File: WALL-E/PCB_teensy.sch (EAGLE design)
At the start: 44 parts

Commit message: added silkscreen to i2c headers
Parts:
- renumbered U$4 to U4
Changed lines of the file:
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@@
 <parts>
 <part name="U$2" library="WALL-E_Parts" deviceset="TACTILE-SWITCH-1825910-7" device=""/>
-<part name="U$4" library="WALL-E_Parts" deviceset="R-78E5.0-0.5" device=""/>
+<part name="U4" library="WALL-E_Parts" deviceset="R-78E5.0-0.5" device=""/>
 <part name="U$5" library="WALL-E_Parts" deviceset="LM3940" device=""/>
 <part name="U$6" library="adafruit" library_urn="urn:adsk.eagle:library:420" deviceset="2.1MMJACK" device="THM"/>
@@
 <instances>
 <instance part="U$2" gate="G$1" x="60.96" y="15.24"/>
-<instance part="U$4" gate="G$1" x="-93.98" y="48.26"/>
+<instance part="U4" gate="G$1" x="-93.98" y="48.26"/>
 <instance part="U$5" gate="G$1" x="-58.42" y="43.18"/>
 <instance part="U$6" gate="G$1" x="-124.46" y="71.12"/>
@@
 <pinref part="U$6" gate="G$1" pin="RING"/>
 <wire x1="-119.38" y1="63.5" x2="-119.38" y2="68.58" width="0.1524" layer="91"/>
-<pinref part="U$4" gate="G$1" pin="VIN"/>
+<pinref part="U4" gate="G$1" pin="VIN"/>
 <wire x1="-119.38" y1="68.58" x2="-109.22" y2="68.58" width="0.1524" layer="91"/>
 <wire x1="-109.22" y1="68.58" x2="-106.68" y2="68.58" width="0.1524" layer="91"/>
@@
 <net name="5V" class="0">
 <segment>
-<pinref part="U$4" gate="G$1" pin="VOUT"/>
+<pinref part="U4" gate="G$1" pin="VOUT"/>
 <wire x1="-81.28" y1="48.26" x2="-76.2" y2="48.26" width="0.1524" layer="91"/>
 <wire x1="-76.2" y1="48.26" x2="-76.2" y2="83.82" width="0.1524" layer="91"/>
@@
 <net name="N$1" class="0">
 <segment>
-<pinref part="U$4" gate="G$1" pin="GND"/>
+<pinref part="U4" gate="G$1" pin="GND"/>
 <pinref part="C4" gate="G$1" pin="1"/>
 <pinref part="TP13" gate="G$1" pin="TP"/>

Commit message: Finished labeling the silkscreen for everything.
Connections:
- removed net N$8: J2.2
- net GND: now also J2.2
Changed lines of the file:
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@@
 <label x="35.56" y="27.94" size="1.778" layer="95"/>
+</segment>
+<segment>
+<pinref part="J2" gate="G$1" pin="2"/>
+<wire x1="-48.26" y1="104.14" x2="-48.26" y2="99.06" width="0.1524" layer="91"/>
 </segment>
 </net>
@@
 </segment>
 </net>
-<net name="N$8" class="0">
-<segment>
-<pinref part="J2" gate="G$1" pin="2"/>
-<wire x1="-48.26" y1="104.14" x2="-48.26" y2="99.06" width="0.1524" layer="91"/>
-</segment>
-</net>

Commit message: removed some test pins
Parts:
- removed TP1, TP3: PTR1B2,54, testpad:PTR1B2,54
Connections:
- net +12V: no longer TP1.TP
- net 5V: no longer TP3.TP
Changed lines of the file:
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@@
 <part name="C5" library="adafruit" library_urn="urn:adsk.eagle:library:420" deviceset="C-US" device="C0805"/>
 <part name="R2" library="adafruit" library_urn="urn:adsk.eagle:library:420" deviceset="R-US_" device="R0805"/>
-<part name="TP1" library="testpad" library_urn="urn:adsk.eagle:library:385" deviceset="PTR1" device="B2,54" package3d_urn="urn:adsk.eagle:package:27948/1"/>
 <part name="TP2" library="testpad" library_urn="urn:adsk.eagle:library:385" deviceset="PTR1" device="B2,54" package3d_urn="urn:adsk.eagle:package:27948/1"/>
-<part name="TP3" library="testpad" library_urn="urn:adsk.eagle:library:385" deviceset="PTR1" device="B2,54" package3d_urn="urn:adsk.eagle:package:27948/1"/>
 <part name="TP10" library="testpad" library_urn="urn:adsk.eagle:library:385" deviceset="PTR1" device="B2,54" package3d_urn="urn:adsk.eagle:package:27948/1"/>
 <part name="TP11" library="testpad" library_urn="urn:adsk.eagle:library:385" deviceset="PTR1" device="B2,54" package3d_urn="urn:adsk.eagle:package:27948/1"/>
@@
 <instance part="C5" gate="G$1" x="48.26" y="5.08"/>
 <instance part="R2" gate="G$1" x="50.8" y="25.4" rot="R90"/>
-<instance part="TP1" gate="G$1" x="-109.22" y="66.04"/>
 <instance part="TP2" gate="G$1" x="-66.04" y="81.28"/>
-<instance part="TP3" gate="G$1" x="-66.04" y="12.7"/>
 <instance part="TP10" gate="G$1" x="30.48" y="17.78"/>
 <instance part="TP11" gate="G$1" x="40.64" y="2.54"/>
@@
 <wire x1="-119.38" y1="63.5" x2="-119.38" y2="68.58" width="0.1524" layer="91"/>
 <pinref part="U4" gate="G$1" pin="VIN"/>
-<wire x1="-119.38" y1="68.58" x2="-109.22" y2="68.58" width="0.1524" layer="91"/>
-<wire x1="-109.22" y1="68.58" x2="-106.68" y2="68.58" width="0.1524" layer="91"/>
+<wire x1="-119.38" y1="68.58" x2="-106.68" y2="68.58" width="0.1524" layer="91"/>
 <wire x1="-106.68" y1="68.58" x2="-106.68" y2="48.26" width="0.1524" layer="91"/>
 <junction x="-119.38" y="68.58"/>
 <pinref part="P+1" gate="1" pin="+12V"/>
-<pinref part="TP1" gate="G$1" pin="TP"/>
-<junction x="-109.22" y="68.58"/>
 </segment>
 <segment>
@@
 <junction x="-76.2" y="48.26"/>
 <pinref part="U$5" gate="G$1" pin="P$1"/>
-<wire x1="-76.2" y1="33.02" x2="-66.04" y2="33.02" width="0.1524" layer="91"/>
+<wire x1="-76.2" y1="33.02" x2="-63.5" y2="33.02" width="0.1524" layer="91"/>
 <pinref part="C1" gate="G$1" pin="1"/>
 <junction x="-76.2" y="33.02"/>
 <pinref part="TP2" gate="G$1" pin="TP"/>
-<pinref part="TP3" gate="G$1" pin="TP"/>
-<wire x1="-66.04" y1="33.02" x2="-63.5" y2="33.02" width="0.1524" layer="91"/>
-<wire x1="-66.04" y1="15.24" x2="-66.04" y2="33.02" width="0.1524" layer="91"/>
-<junction x="-66.04" y="33.02"/>
 <label x="-76.2" y="48.26" size="1.778" layer="95"/>
 </segment>

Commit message: added tp1 for 3.3V
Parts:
- added TP1: PTR1B2,54, testpad:PTR1B2,54
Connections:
- net 3.3V: now also TP1.TP
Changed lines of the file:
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@@
 <part name="R7" library="adafruit" library_urn="urn:adsk.eagle:library:420" deviceset="R-US_" device="R0805"/>
 <part name="R8" library="adafruit" library_urn="urn:adsk.eagle:library:420" deviceset="R-US_" device="R0805"/>
+<part name="TP1" library="testpad" library_urn="urn:adsk.eagle:library:385" deviceset="PTR1" device="B2,54" package3d_urn="urn:adsk.eagle:package:27948/1"/>
 </parts>
 <sheets>
@@
 <instance part="R7" gate="G$1" x="88.9" y="66.04"/>
 <instance part="R8" gate="G$1" x="88.9" y="60.96"/>
+<instance part="TP1" gate="G$1" x="-50.8" y="5.08"/>
 </instances>
 <busses>
@@
 <segment>
 <pinref part="U$5" gate="G$1" pin="P$3"/>
-<wire x1="-53.34" y1="33.02" x2="-45.72" y2="33.02" width="0.1524" layer="91"/>
+<wire x1="-53.34" y1="33.02" x2="-50.8" y2="33.02" width="0.1524" layer="91"/>
 <pinref part="C2" gate="G$1" pin="1"/>
 <label x="-45.72" y="35.56" size="1.778" layer="95"/>
-</segment>
-<segment>
+<pinref part="TP1" gate="G$1" pin="TP"/>
+<wire x1="-50.8" y1="33.02" x2="-45.72" y2="33.02" width="0.1524" layer="91"/>
+<wire x1="-50.8" y1="7.62" x2="-50.8" y2="33.02" width="0.1524" layer="91"/>
+<junction x="-50.8" y="33.02"/>
+</segment>
+<segment>

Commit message: removed some unneeded bypass caps
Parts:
- removed C3, C4, C5: (no value), adafruit:C-USC0805
- removed TP11, TP12, TP13: PTR1B2,54, testpad:PTR1B2,54
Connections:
- removed net N$1: C4.1, TP13.TP, U4.GND
- removed net N$3: C3.1, TP12.TP, U$5.P$2
- removed net N$5: C5.1, TP11.TP, U$2.P$3
- net GND: now also U$2.P$3, U$5.P$2, U4.GND; no longer C3.2, C4.2, C5.2
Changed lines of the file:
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@@
 <part name="GND7" library="supply1" library_urn="urn:adsk.eagle:library:371" deviceset="GND" device=""/>
 <part name="GND8" library="supply1" library_urn="urn:adsk.eagle:library:371" deviceset="GND" device=""/>
-<part name="C3" library="adafruit" library_urn="urn:adsk.eagle:library:420" deviceset="C-US" device="C0805"/>
 <part name="GND3" library="supply1" library_urn="urn:adsk.eagle:library:371" deviceset="GND" device=""/>
-<part name="C4" library="adafruit" library_urn="urn:adsk.eagle:library:420" deviceset="C-US" device="C0805"/>
 <part name="GND10" library="supply1" library_urn="urn:adsk.eagle:library:371" deviceset="GND" device=""/>
 <part name="GND11" library="supply1" library_urn="urn:adsk.eagle:library:371" deviceset="GND" device=""/>
 <part name="GND12" library="supply1" library_urn="urn:adsk.eagle:library:371" deviceset="GND" device=""/>
-<part name="C5" library="adafruit" library_urn="urn:adsk.eagle:library:420" deviceset="C-US" device="C0805"/>
 <part name="R2" library="adafruit" library_urn="urn:adsk.eagle:library:420" deviceset="R-US_" device="R0805"/>
 <part name="TP2" library="testpad" library_urn="urn:adsk.eagle:library:385" deviceset="PTR1" device="B2,54" package3d_urn="urn:adsk.eagle:package:27948/1"/>
 <part name="TP10" library="testpad" library_urn="urn:adsk.eagle:library:385" deviceset="PTR1" device="B2,54" package3d_urn="urn:adsk.eagle:package:27948/1"/>
-<part name="TP11" library="testpad" library_urn="urn:adsk.eagle:library:385" deviceset="PTR1" device="B2,54" package3d_urn="urn:adsk.eagle:package:27948/1"/>
-<part name="TP12" library="testpad" library_urn="urn:adsk.eagle:library:385" deviceset="PTR1" device="B2,54" package3d_urn="urn:adsk.eagle:package:27948/1"/>
-<part name="TP13" library="testpad" library_urn="urn:adsk.eagle:library:385" deviceset="PTR1" device="B2,54" package3d_urn="urn:adsk.eagle:package:27948/1"/>
 <part name="J1" library="con-amp" library_urn="urn:adsk.eagle:library:127" deviceset="MTA04-100" device=""/>
 <part name="J2" library="con-amp" library_urn="urn:adsk.eagle:library:127" deviceset="MTA04-100" device=""/>
@@
 <instance part="GND1" gate="1" x="-119.38" y="78.74" rot="R180"/>
 <instance part="C2" gate="G$1" x="-45.72" y="30.48"/>
-<instance part="GND2" gate="1" x="-93.98" y="30.48"/>
+<instance part="GND2" gate="1" x="-93.98" y="38.1"/>
 <instance part="GND4" gate="1" x="-58.42" y="58.42" rot="R180"/>
 <instance part="GND7" gate="1" x="-45.72" y="22.86"/>
 <instance part="GND8" gate="1" x="-76.2" y="22.86"/>
-<instance part="C3" gate="G$1" x="-58.42" y="30.48"/>
-<instance part="GND3" gate="1" x="-58.42" y="22.86"/>
-<instance part="C4" gate="G$1" x="-93.98" y="38.1"/>
+<instance part="GND3" gate="1" x="-58.42" y="27.94"/>
 <instance part="GND10" gate="1" x="78.74" y="20.32" rot="R90"/>
 <instance part="GND11" gate="1" x="78.74" y="15.24" rot="R90"/>
-<instance part="GND12" gate="1" x="48.26" y="-2.54"/>
-<instance part="C5" gate="G$1" x="48.26" y="5.08"/>
+<instance part="GND12" gate="1" x="48.26" y="12.7"/>
 <instance part="R2" gate="G$1" x="50.8" y="25.4" rot="R90"/>
 <instance part="TP2" gate="G$1" x="-66.04" y="81.28"/>
 <instance part="TP10" gate="G$1" x="30.48" y="17.78"/>
-<instance part="TP11" gate="G$1" x="40.64" y="2.54"/>
-<instance part="TP12" gate="G$1" x="-55.88" y="5.08"/>
-<instance part="TP13" gate="G$1" x="-101.6" y="30.48"/>
 <instance part="J1" gate="G$1" x="-73.66" y="106.68"/>
 <instance part="J2" gate="G$1" x="-48.26" y="106.68"/>
@@
 </segment>
 <segment>
-<pinref part="C3" gate="G$1" pin="2"/>
-<pinref part="GND3" gate="1" pin="GND"/>
-</segment>
-<segment>
-<pinref part="GND2" gate="1" pin="GND"/>
-<pinref part="C4" gate="G$1" pin="2"/>
-</segment>
-<segment>
 <pinref part="U$2" gate="G$1" pin="P$2"/>
 <pinref part="GND10" gate="1" pin="GND"/>
@@
 <pinref part="U$2" gate="G$1" pin="P$4"/>
 <pinref part="GND11" gate="1" pin="GND"/>
-</segment>
-<segment>
-<pinref part="GND12" gate="1" pin="GND"/>
-<pinref part="C5" gate="G$1" pin="2"/>
 </segment>
 <segment>
@@
 <pinref part="J2" gate="G$1" pin="2"/>
 <wire x1="-48.26" y1="104.14" x2="-48.26" y2="99.06" width="0.1524" layer="91"/>
+</segment>
+<segment>
+<pinref part="U$5" gate="G$1" pin="P$2"/>
+<pinref part="GND3" gate="1" pin="GND"/>
+<wire x1="-58.42" y1="30.48" x2="-58.42" y2="33.02" width="0.1524" layer="91"/>
+</segment>
+<segment>
+<pinref part="U4" gate="G$1" pin="GND"/>
+<pinref part="GND2" gate="1" pin="GND"/>
+</segment>
+<segment>
+<pinref part="U$2" gate="G$1" pin="P$3"/>
+<pinref part="GND12" gate="1" pin="GND"/>
+<wire x1="48.26" y1="15.24" x2="50.8" y2="15.24" width="0.1524" layer="91"/>
 </segment>
 </net>
@@
 </segment>
 </net>
-<net name="N$1" class="0">
-<segment>
-<pinref part="U4" gate="G$1" pin="GND"/>
-<pinref part="C4" gate="G$1" pin="1"/>
-<pinref part="TP13" gate="G$1" pin="TP"/>
-<wire x1="-101.6" y1="33.02" x2="-101.6" y2="40.64" width="0.1524" layer="91"/>
-<wire x1="-101.6" y1="40.64" x2="-93.98" y2="40.64" width="0.1524" layer="91"/>
-<junction x="-93.98" y="40.64"/>
-</segment>
-</net>
-<net name="N$3" class="0">
-<segment>
-<pinref part="C3" gate="G$1" pin="1"/>
-<pinref part="U$5" gate="G$1" pin="P$2"/>
-<wire x1="-58.42" y1="33.02" x2="-55.88" y2="33.02" width="0.1524" layer="91"/>
-<wire x1="-55.88" y1="33.02" x2="-55.88" y2="7.62" width="0.1524" layer="91"/>
-<junction x="-58.42" y="33.02"/>
-<pinref part="TP12" gate="G$1" pin="TP"/>
-</segment>
-</net>
 <net name="N$4" class="0">
 <segment>
@@
 </segment>
 </net>
-<net name="N$5" class="0">
-<segment>
-<pinref part="C5" gate="G$1" pin="1"/>
-<pinref part="U$2" gate="G$1" pin="P$3"/>
-<wire x1="48.26" y1="7.62" x2="48.26" y2="15.24" width="0.1524" layer="91"/>
-<wire x1="48.26" y1="15.24" x2="50.8" y2="15.24" width="0.1524" layer="91"/>
-<pinref part="TP11" gate="G$1" pin="TP"/>
-<wire x1="40.64" y1="5.08" x2="40.64" y2="15.24" width="0.1524" layer="91"/>
-<wire x1="40.64" y1="15.24" x2="48.26" y2="15.24" width="0.1524" layer="91"/>
-<junction x="48.26" y="15.24"/>
-</segment>
-</net>

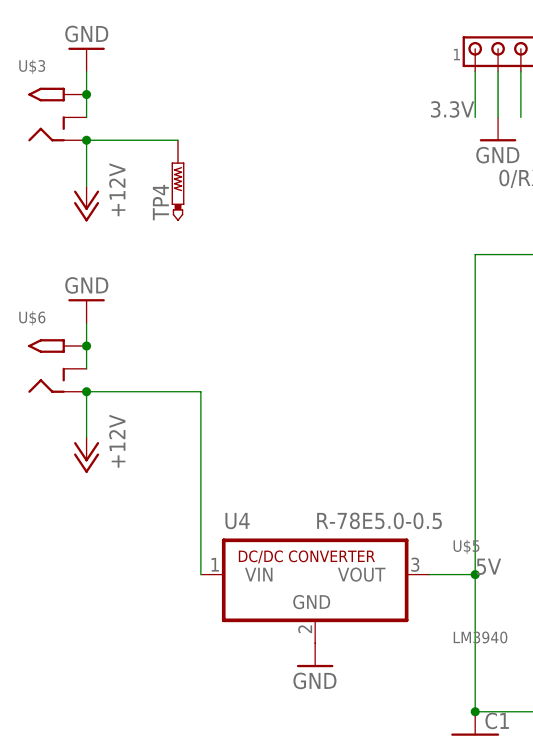
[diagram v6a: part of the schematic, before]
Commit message: fixes power jack and tactile switch
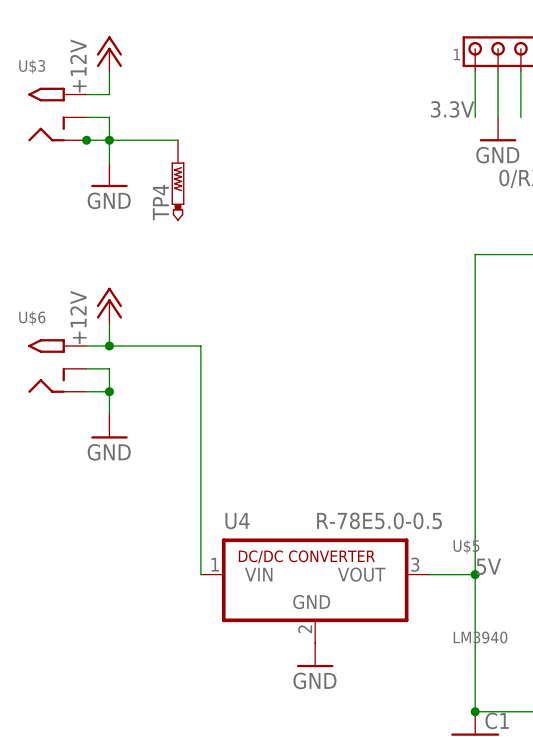
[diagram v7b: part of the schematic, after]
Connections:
- net +12V: now also U$3.TIP, U$6.TIP; no longer TP4.TP, U$3.RING, U$6.RING
- net GND: now also TP4.TP, U$3.RING, U$6.RING; no longer U$3.TIP, U$6.TIP
